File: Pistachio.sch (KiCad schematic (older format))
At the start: 194 parts, among them J1 AudioJack4, J2 AudioJack4, SW1 SW_Push, SW10 SW_Push, SW11 SW_Push, SW12 SW_Push, SW13 SW_Push, SW14 SW_Push, SW15 SW_Push, SW16 SW_Push, SW17 SW_Push, SW18 SW_Push, SW19 SW_Push, SW2 SW_Push, SW20 SW_Push, SW21 SW_Push, SW22 SW_Push, SW23 SW_Push, SW24 SW_Push, SW25 SW_Push, SW26 SW_Push, SW27 SW_Push, SW28 SW_Push, SW29 SW_Push, SW3 SW_Push, SW30 SW_Push, SW31 SW_Push, SW32 SW_Push, SW33 SW_Push, SW34 SW_Push, SW35 SW_Push, SW36 SW_Push, SW37 SW_Push, SW38 SW_Push, SW39 SW_Push, SW4 SW_Push, SW40 SW_Push, SW41 SW_Push, SW42 SW_Push, SW43 SW_Push, SW44 SW_Push, SW45 SW_Push, SW46 SW_Push, SW47 SW_Push, SW48 SW_Push, SW49 SW_Push, SW5 SW_Push, SW50 SW_Push, SW51 SW_Push, SW52 SW_Push, SW53 SW_Push, SW54 SW_Push, SW55 SW_Push, SW56 SW_Push, SW57 SW_Push, SW58 SW_Push, SW59 SW_Push, SW6 SW_Push, SW60 SW_Push, SW61 SW_Push, SW62 SW_Push, SW63 SW_Push, SW64 SW_Push, SW65 SW_Push, SW66 SW_Push, SW67 SW_Push, SW68 SW_Push, SW69 SW_Push, SW7 SW_Push, SW70 SW_Push, SW71 SW_Push, SW72 SW_Push, SW73 SW_Push, SW74 SW_Push, SW75 SW_Push, SW76 SW_Push, SW77 SW_Push, SW78 SW_Push, SW79 SW_Push, SW8 SW_Push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

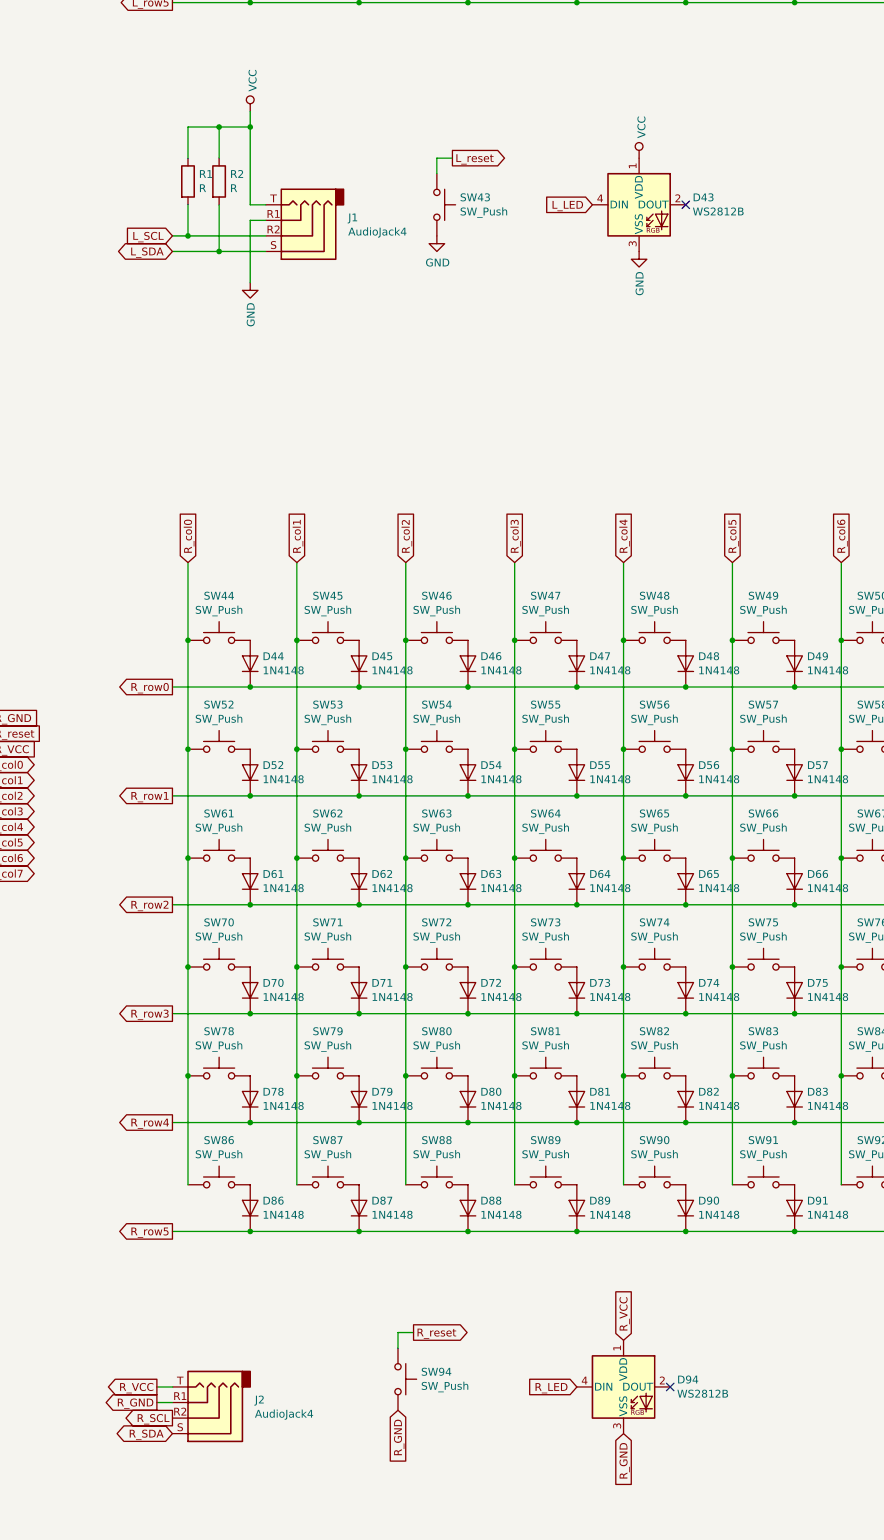
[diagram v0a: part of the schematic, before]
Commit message: サブモジュール整理 一旦配線完了
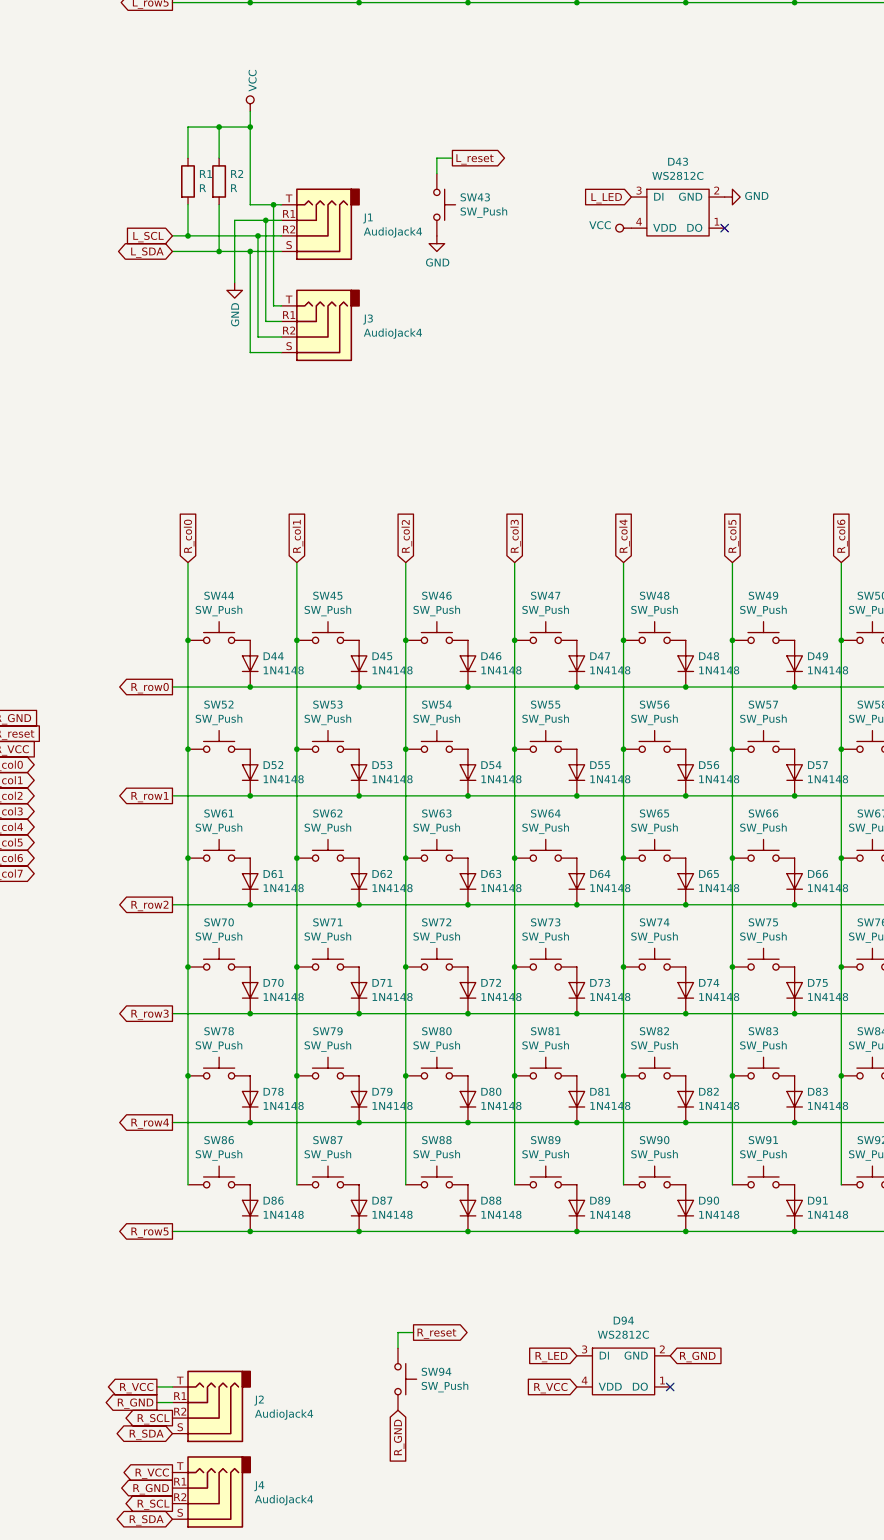
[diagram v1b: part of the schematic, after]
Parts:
- removed D43, D94: WS2812B, CrumpPrints.pretty:WS2812-2020, symbol LED:WS2812B
- added D43, D94: WS2812C, keyboard:WS2812C-2020, symbol keyboard:WS2812C
- added J3, J4: AudioJack4, keyboard:MJ-4PP-9_1side, symbol Connector:AudioJack4
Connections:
- net GND: now also D43.2 (GND), J3.R1
- net L_LED: now also D43.3 (DI)
- net L_SCL: now also J3.R2
- net L_SDA: now also J3.S
- net R_GND: now also D94.2 (GND), J4.R1
- net R_LED: now also D94.3 (DI)
- net R_SCL: now also J4.R2
- net R_SDA: now also J4.S
- net R_VCC: now also D94.4 (VDD), J4.T
- net VCC: now also D43.4 (VDD), J3.T
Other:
- moved on the sheet: J1
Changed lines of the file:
@@
 $EndComp
 $Comp
-L power:GND #PWR08
+L power:GND #PWR09
 U 1 1 5EEEECF8
 P 5700 6600
-F 0 "#PWR08" H 5700 6350 50  0001 C CNN
+F 0 "#PWR09" H 5700 6350 50  0001 C CNN
 F 1 "GND" H 5705 6427 50  0000 C CNN
 F 2 "" H 5700 6600 50  0001 C CNN
@@
 L power:GND #PWR010
 U 1 1 5EDF2EED
-P 4500 6900
-F 0 "#PWR010" H 4500 6650 50  0001 C CNN
-F 1 "GND" V 4505 6772 50  0000 R CNN
-F 2 "" H 4500 6900 50  0001 C CNN
-F 3 "" H 4500 6900 50  0001 C CNN
-	1    4500 6900
-	1    0    0    -1
-$EndComp
-Wire Wire Line
-	4500 6400 4600 6400
-Wire Wire Line
-	4600 6500 4500 6500
+P 4400 6900
+F 0 "#PWR010" H 4400 6650 50  0001 C CNN
+F 1 "GND" V 4405 6772 50  0000 R CNN
+F 2 "" H 4400 6900 50  0001 C CNN
+F 3 "" H 4400 6900 50  0001 C CNN
+	1    4400 6900
+	1    0    0    -1
+$EndComp
 NoConn ~ 2800 1500
 Text GLabel 4100 8700 1    50   Input ~ 0
@@
 L Connector:AudioJack4 J1
 U 1 1 5EDEE7C7
-P 4800 6600
-F 0 "J1" H 4470 6483 50  0000 R CNN
-F 1 "AudioJack4" H 4470 6574 50  0000 R CNN
-F 2 "keyboard:MJ-4PP-9_1side" H 4800 6600 50  0001 C CNN
-F 3 "~" H 4800 6600 50  0001 C CNN
-	1    4800 6600
+P 4900 6600
+F 0 "J1" H 4570 6483 50  0000 R CNN
+F 1 "AudioJack4" H 4570 6574 50  0000 R CNN
+F 2 "keyboard:MJ-4PP-9_1side" H 4900 6600 50  0001 C CNN
+F 3 "~" H 4900 6600 50  0001 C CNN
+	1    4900 6600
 	-1   0    0    1
 $EndComp
 Wire Wire Line
-	4500 6500 4500 6900
-Wire Wire Line
 	4000 6600 4100 6600
-Wire Wire Line
-	4600 6700 4300 6700
 Connection ~ 4100 6600
 Wire Wire Line
 	4100 6400 4100 6600
-Wire Wire Line
-	4100 6600 4600 6600
 Wire Wire Line
 	4300 6400 4300 6700
@@
 	4500 5800 4500 5900
 $Comp
-L LED:WS2812B D43
-U 1 1 5F0A7845
-P 7000 6400
-F 0 "D43" H 7344 6446 50  0000 L CNN
-F 1 "WS2812B" H 7344 6355 50  0000 L CNN
-F 2 "CrumpPrints.pretty:WS2812-2020" H 7050 6100 50  0001 L TNN
-F 3 "https://cdn-shop.adafruit.com/datasheets/WS2812B.pdf" H 7100 6025 50  0001 L TNN
-	1    7000 6400
-	1    0    0    -1
-$EndComp
-$Comp
-L LED:WS2812B D94
-U 1 1 5F0A8A32
-P 6900 14000
-F 0 "D94" H 7244 14046 50  0000 L CNN
-F 1 "WS2812B" H 7244 13955 50  0000 L CNN
-F 2 "CrumpPrints.pretty:WS2812-2020" H 6950 13700 50  0001 L TNN
-F 3 "https://cdn-shop.adafruit.com/datasheets/WS2812B.pdf" H 7000 13625 50  0001 L TNN
-	1    6900 14000
-	1    0    0    -1
-$EndComp
-$Comp
-L power:VCC #PWR07
+L power:VCC #PWR08
 U 1 1 5F0A9D81
-P 7000 6100
-F 0 "#PWR07" H 7000 5950 50  0001 C CNN
-F 1 "VCC" V 7017 6228 50  0000 L CNN
-F 2 "" H 7000 6100 50  0001 C CNN
-F 3 "" H 7000 6100 50  0001 C CNN
-	1    7000 6100
-	1    0    0    -1
-$EndComp
-$Comp
-L power:GND #PWR09
+P 6950 6550
+F 0 "#PWR08" H 6950 6400 50  0001 C CNN
+F 1 "VCC" V 6967 6678 50  0000 L CNN
+F 2 "" H 6950 6550 50  0001 C CNN
+F 3 "" H 6950 6550 50  0001 C CNN
+	1    6950 6550
+	0    -1   -1   0
+$EndComp
+$Comp
+L power:GND #PWR07
 U 1 1 5F0AB861
-P 7000 6700
-F 0 "#PWR09" H 7000 6450 50  0001 C CNN
-F 1 "GND" V 7005 6572 50  0000 R CNN
-F 2 "" H 7000 6700 50  0001 C CNN
-F 3 "" H 7000 6700 50  0001 C CNN
-	1    7000 6700
-	1    0    0    -1
-$EndComp
-NoConn ~ 7300 6400
+P 7550 6350
+F 0 "#PWR07" H 7550 6100 50  0001 C CNN
+F 1 "GND" V 7555 6222 50  0000 R CNN
+F 2 "" H 7550 6350 50  0001 C CNN
+F 3 "" H 7550 6350 50  0001 C CNN
+	1    7550 6350
+	0    -1   -1   0
+$EndComp
+NoConn ~ 7550 6550
 Text GLabel 1400 1600 0    50   Output ~ 0
 L_LED
-Text GLabel 6700 6400 0    50   Input ~ 0
+Text GLabel 6950 6350 0    50   Input ~ 0
 L_LED
-Text GLabel 6900 13700 1    50   Input ~ 0
+Text GLabel 6600 14000 0    50   Input ~ 0
 R_VCC
-Text GLabel 6900 14300 3    50   Input ~ 0
+Text GLabel 7200 13800 2    50   Input ~ 0
 R_GND
 NoConn ~ 7200 14000
 Text GLabel 1400 9700 0    50   Output ~ 0
 R_LED
-Text GLabel 6600 14000 0    50   Input ~ 0
+Text GLabel 6600 13800 0    50   Input ~ 0
 R_LED
 $Comp
@@
 $Comp
 L keyboard:ProMicro U1
-U 1 1 5F0A8ABF
+U 1 1 5F0DBAE1
 P 2100 2250
 F 0 "U1" H 2100 3287 60  0000 C CNN
@@
 $Comp
 L keyboard:ProMicro U2
-U 1 1 5F0A9D1C
+U 1 1 5F0DCE83
 P 2100 10350
 F 0 "U2" H 2100 11387 60  0000 C CNN
@@
 $EndComp
 Connection ~ 1400 9800
+$Comp
+L keyboard:WS2812C D94
+U 1 1 5F0DEB29
+P 6900 13900
+F 0 "D94" H 6900 14225 50  0000 C CNN
+F 1 "WS2812C" H 6900 14134 50  0000 C CNN
+F 2 "keyboard:WS2812C-2020" H 6900 13950 50  0001 C CNN
+F 3 "" H 6900 13950 50  0001 C CNN
+	1    6900 13900
+	1    0    0    -1
+$EndComp
+$Comp
+L keyboard:WS2812C D43
+U 1 1 5F111E47
+P 7250 6450
+F 0 "D43" H 7250 6775 50  0000 C CNN
+F 1 "WS2812C" H 7250 6684 50  0000 C CNN
+F 2 "keyboard:WS2812C-2020" H 7250 6500 50  0001 C CNN
+F 3 "" H 7250 6500 50  0001 C CNN
+	1    7250 6450
+	1    0    0    -1
+$EndComp
+$Comp
+L Connector:AudioJack4 J3
+U 1 1 5F0D424A
+P 4900 7250
+F 0 "J3" H 4570 7133 50  0000 R CNN
+F 1 "AudioJack4" H 4570 7224 50  0000 R CNN
+F 2 "keyboard:MJ-4PP-9_1side" H 4900 7250 50  0001 C CNN
+F 3 "~" H 4900 7250 50  0001 C CNN
+	1    4900 7250
+	-1   0    0    1
+$EndComp
+Wire Wire Line
+	4500 6400 4650 6400
+Wire Wire Line
+	4100 6600 4550 6600
+Wire Wire Line
+	4300 6700 4500 6700
+Wire Wire Line
+	4700 7050 4650 7050
+Wire Wire Line
+	4650 7050 4650 6400
+Connection ~ 4650 6400
+Wire Wire Line
+	4650 6400 4700 6400
+Wire Wire Line
+	4600 6500 4600 7150
+Wire Wire Line
+	4600 7150 4700 7150
+Connection ~ 4600 6500
+Wire Wire Line
+	4600 6500 4700 6500
+Wire Wire Line
+	4550 6600 4550 7250
+Wire Wire Line
+	4550 7250 4700 7250
+Connection ~ 4550 6600
+Wire Wire Line
+	4550 6600 4700 6600
+Wire Wire Line
+	4400 6500 4400 6900
+Wire Wire Line
+	4400 6500 4600 6500
+Wire Wire Line
+	4500 6700 4500 7350
+Wire Wire Line
+	4500 7350 4700 7350
+Connection ~ 4500 6700
+Wire Wire Line
+	4500 6700 4700 6700
+$Comp
+L Connector:AudioJack4 J4
+U 1 1 5F159D3D
+P 4200 14750
+F 0 "J4" H 3870 14633 50  0000 R CNN
+F 1 "AudioJack4" H 3870 14724 50  0000 R CNN
+F 2 "keyboard:MJ-4PP-9_1side" H 4200 14750 50  0001 C CNN
+F 3 "~" H 4200 14750 50  0001 C CNN
+	1    4200 14750
+	-1   0    0    1
+$EndComp
+Text GLabel 4000 14550 0    50   Output ~ 0
+R_VCC
+Text GLabel 4000 14650 0    50   Output ~ 0
+R_GND
+Text GLabel 4000 14750 0    50   Output ~ 0
+R_SCL
+Text GLabel 4000 14850 0    50   BiDi ~ 0
+R_SDA
 $EndSCHEMATC
